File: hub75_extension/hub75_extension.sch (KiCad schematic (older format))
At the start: 40 parts, among them J1 Screw_Terminal_01x02, J2 Screw_Terminal_01x02, J3 Barrel_Jack_Switch, J4 Screw_Terminal_01x02, J5 Screw_Terminal_01x02, J6 Barrel_Jack_Switch, J7 Screw_Terminal_01x02, J8 Screw_Terminal_01x02, J9 USB_B_Micro, U1 74HC595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

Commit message: Schematic improvements for the HUB75 board
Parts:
- added J_IN1: HUB75, Connector_IDC:IDC-Header_2x08_P2.54mm_Vertical, symbol HUB75:HUB75
- J_DS1: footprint Connector_PinHeader_2.54mm:PinHeader_2x09_P2.54mm_Vertical -> ds_card_extender:IDC-Header_2x09_P2.54mm_Vertical
- J_HUB12_1: renamed from J_FOUND1; value Found_LED_panel -> HUB12; footprint Connector_IDC:IDC-Header_2x08_P2.54mm_Vertical -> Connector_PinSocket_2.54mm:PinSocket_2x08_P2.54mm_Vertical; symbol Found_LED_panel:Found_LED_panel -> HUB75:HUB12
- J_PANEL1: footprint Connector_IDC:IDC-Header_2x08_P2.54mm_Vertical -> Connector_PinSocket_2.54mm:PinSocket_2x08_P2.54mm_Vertical
- renumbered J_CHAIN1 to J_OUT1
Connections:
- wire segments 217 -> 237
- no-connect marks 19 -> 18
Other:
- moved on the sheet: C1, H1, H2, H3, JP11, JP12, JP13, JP14, JP7, JP8, JP9, TP1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

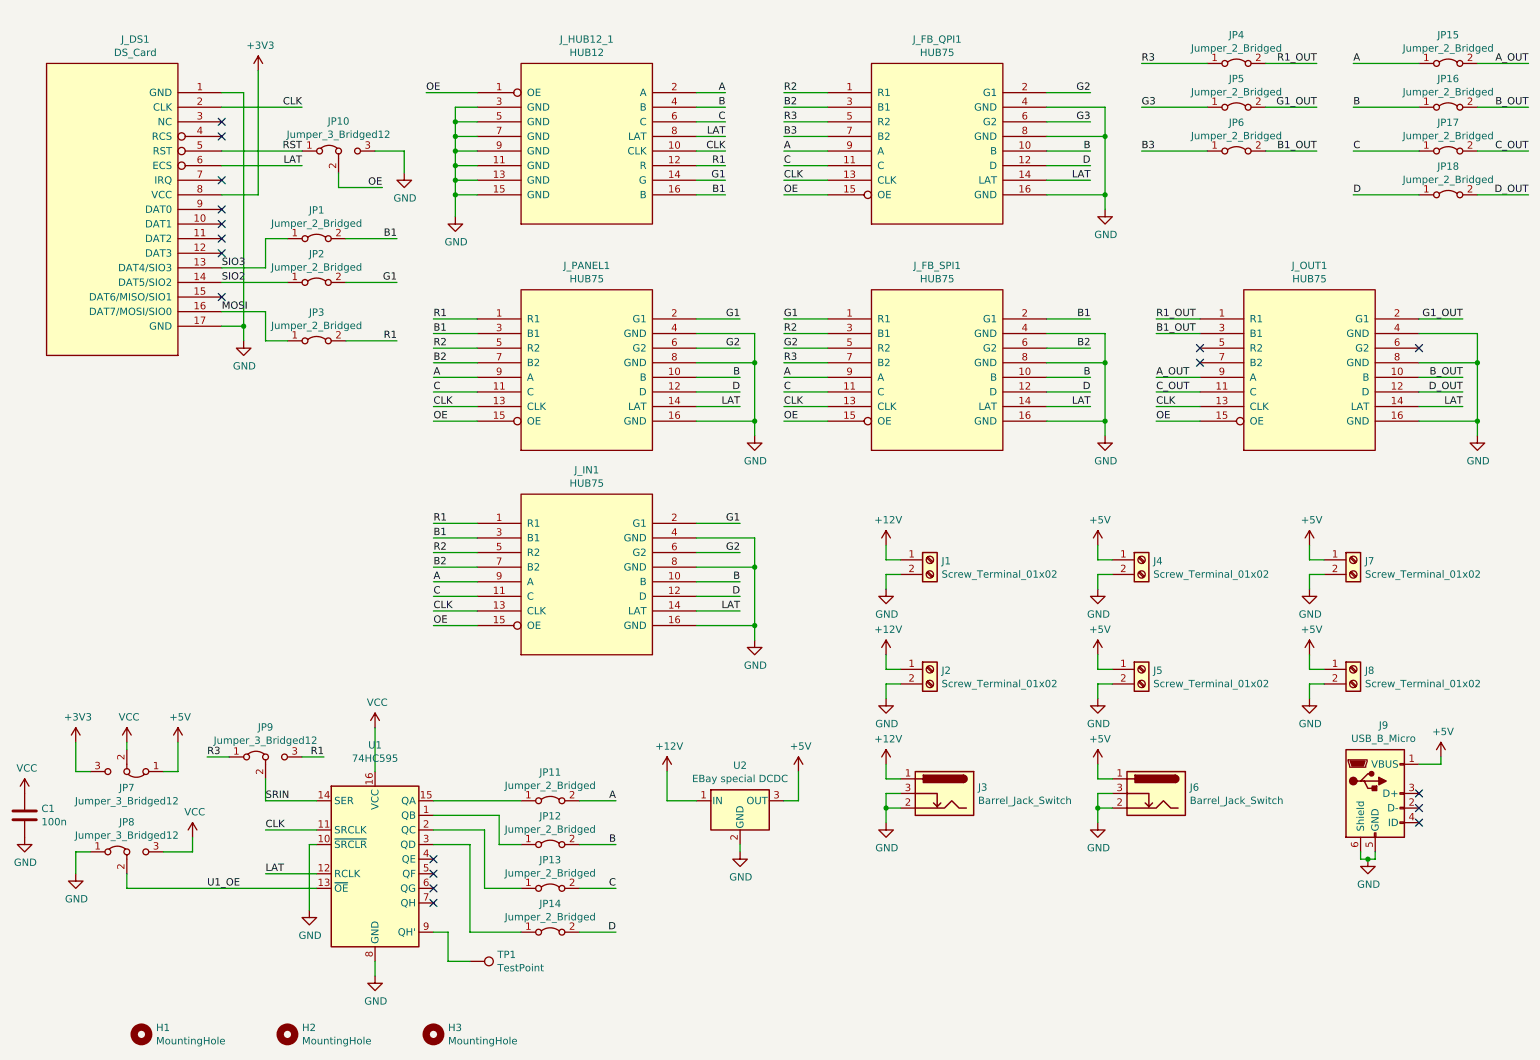
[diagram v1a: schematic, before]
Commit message: Giant schematic update on the HUB75 extension
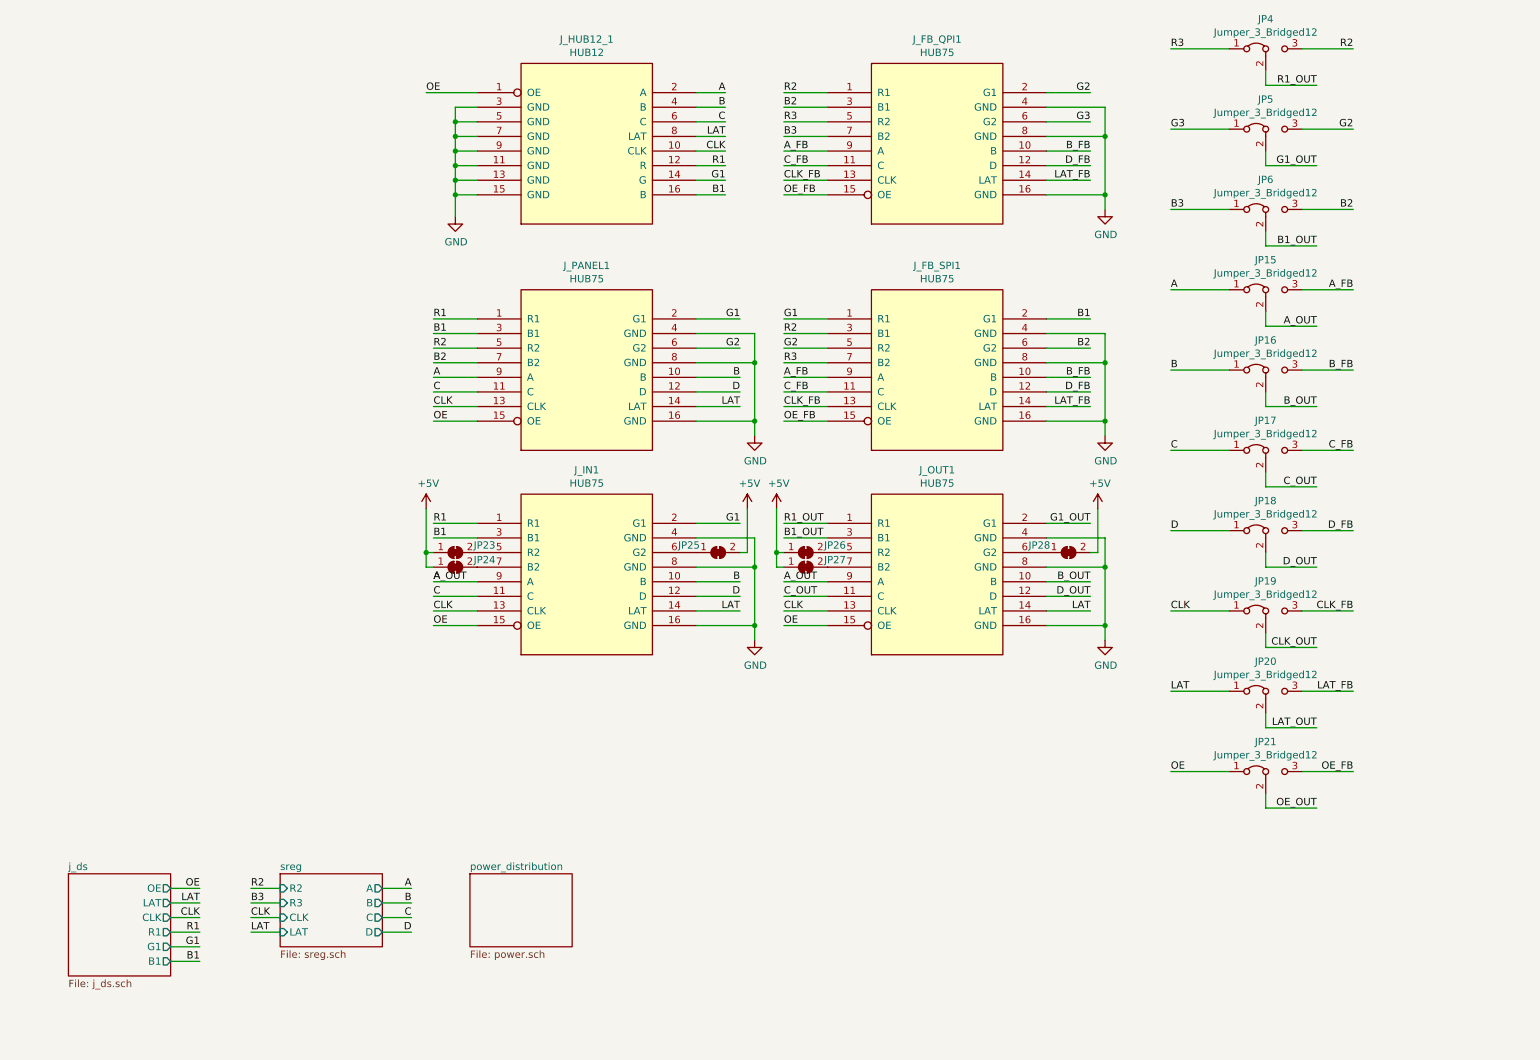
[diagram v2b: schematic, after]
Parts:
- removed C1: 100n, Capacitor_SMD:C_0603_1608Metric_Pad1.08x0.95mm_HandSolder, symbol Device:C
- removed H1, H2, H3: MountingHole, usb_indicator_light:JLC_TOOLING_HOLE, symbol Mechanical:MountingHole
- removed J1, J2, J4, J5, J7, J8: Screw_Terminal_01x02, TerminalBlock:TerminalBlock_bornier-2_P5.08mm, symbol Connector:Screw_Terminal_01x02
- removed J3, J6: Barrel_Jack_Switch, Connector_BarrelJack:BarrelJack_Horizontal, symbol Connector:Barrel_Jack_Switch
- removed J9: USB_B_Micro, Connector_USB:USB_Micro-B_Wuerth_629105150521, symbol Connector:USB_B_Micro
- removed JP1, JP11, JP12, JP13, JP14, JP15, JP16, JP17, JP18, JP2, JP3, JP4, JP5, JP6: Jumper_2_Bridged, Connector_PinHeader_2.54mm:PinHeader_1x02_P2.54mm_Vertical, symbol Jumper:Jumper_2_Bridged
- removed JP10, JP7, JP8, JP9: Jumper_3_Bridged12, Connector_PinHeader_2.54mm:PinHeader_1x03_P2.54mm_Vertical, symbol Jumper:Jumper_3_Bridged12
- removed J_DS1: DS_Card, ds_card_extender:IDC-Header_2x09_P2.54mm_Vertical, symbol ds_card_extender:DS_Card
- removed TP1: TestPoint, Connector_PinHeader_2.54mm:PinHeader_1x01_P2.54mm_Vertical, symbol Connector:TestPoint
- removed U1: 74HC595, Package_SO:SOIC-16_3.9x9.9mm_P1.27mm, symbol 74xx:74HC595
- removed U2: EBay special DCDC, ebay_special_dcdc:ebay_special_dcdc, symbol Regulator_Linear:L7805
- added JP15, JP16, JP17, JP18, JP19, JP20, JP21, JP4, JP5, JP6: Jumper_3_Bridged12, Connector_PinHeader_2.54mm:PinHeader_1x03_P2.54mm_Vertical, symbol Jumper:Jumper_3_Bridged12
- added JP23, JP24, JP25, JP26, JP27, JP28: SolderJumper_2_Bridged, Jumper:SolderJumper-2_P1.3mm_Bridged2Bar_RoundedPad1.0x1.5mm, symbol Jumper:SolderJumper_2_Bridged
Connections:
- net A_OUT is gone; now on net A: J_OUT1.9 (A)
- net +5V: now also JP23.1 (A), JP24.1 (A), JP25.2 (B), JP26.1 (A), JP27.1 (A), JP28.2 (B)
- net A: now also JP15.1 (A), JP15.2 (C); no longer J_FB_QPI1.9 (A), J_FB_SPI1.9 (A)
- net B: now also JP16.1 (A); no longer J_FB_QPI1.10 (B), J_FB_SPI1.10 (B)
- net B1_OUT: now also JP6.2 (C)
- net B2: now also JP6.3 (B); no longer J_IN1.7 (B2)
- net B3: now also JP6.1 (A)
- net B_OUT: now also JP16.2 (C)
- net C: now also JP17.1 (A); no longer J_FB_QPI1.11 (C), J_FB_SPI1.11 (C)
- net CLK: now also JP19.1 (A); no longer J_FB_QPI1.13 (CLK), J_FB_SPI1.13 (CLK)
- net C_OUT: now also JP17.2 (C)
- net D: now also JP18.1 (A); no longer J_FB_QPI1.12 (D), J_FB_SPI1.12 (D)
- net D_OUT: now also JP18.2 (C)
- net G1_OUT: now also JP5.2 (C)
- net G2: now also JP5.3 (B); no longer J_IN1.6 (G2)
- net G3: now also JP5.1 (A)
- net LAT: now also JP20.1 (A); no longer J_FB_QPI1.14 (LAT), J_FB_SPI1.14 (LAT)
- net OE: now also JP21.1 (A); no longer J_FB_QPI1.15 (OE), J_FB_SPI1.15 (OE)
- net R1_OUT: now also JP4.2 (C)
- net R2: now also JP4.3 (B); no longer J_IN1.5 (R2)
- net R3: now also JP4.1 (A)
- net at J_OUT1.5 (R2): now also JP26.2 (B)
- net at J_OUT1.6 (G2): now also JP28.1 (A)
- net at J_OUT1.7 (B2): now also JP27.2 (B)
- new net: JP23.2 (B), J_IN1.5 (R2)
- new net: JP25.1 (A), J_IN1.6 (G2)
- new net: JP24.2 (B), J_IN1.7 (B2)
- new net A_FB: JP15.3 (B), J_FB_QPI1.9 (A), J_FB_SPI1.9 (A)
- new net B_FB: JP16.3 (B), J_FB_QPI1.10 (B), J_FB_SPI1.10 (B)
- new net CLK_FB: JP19.3 (B), J_FB_QPI1.13 (CLK), J_FB_SPI1.13 (CLK)
- new net CLK_OUT: JP19.2 (C)
- new net C_FB: JP17.3 (B), J_FB_QPI1.11 (C), J_FB_SPI1.11 (C)
- new net D_FB: JP18.3 (B), J_FB_QPI1.12 (D), J_FB_SPI1.12 (D)
- new net LAT_FB: JP20.3 (B), J_FB_QPI1.14 (LAT), J_FB_SPI1.14 (LAT)
- new net LAT_OUT: JP20.2 (C)
- new net OE_FB: JP21.3 (B), J_FB_QPI1.15 (OE), J_FB_SPI1.15 (OE)
- new net OE_OUT: JP21.2 (C)
- no-connect marks 18 -> 0
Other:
- moved on the sheet: J_OUT1
